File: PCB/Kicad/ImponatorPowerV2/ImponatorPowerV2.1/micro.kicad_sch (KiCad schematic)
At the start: 7 parts, among them U2 EFM8UB10F16G

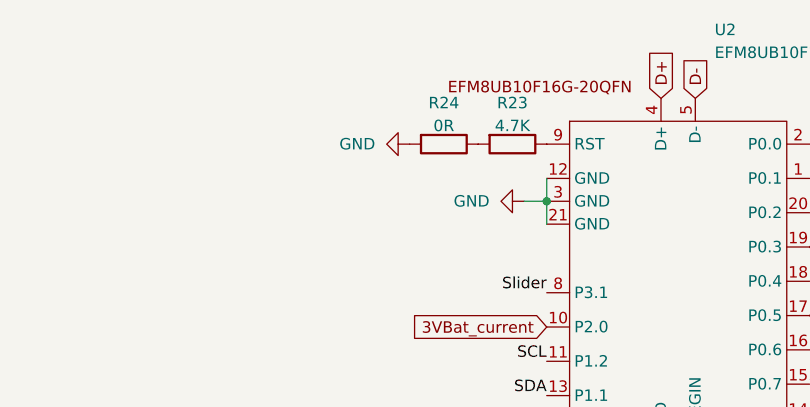
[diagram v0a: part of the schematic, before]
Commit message: 6 layer version of imponatorPower routed.
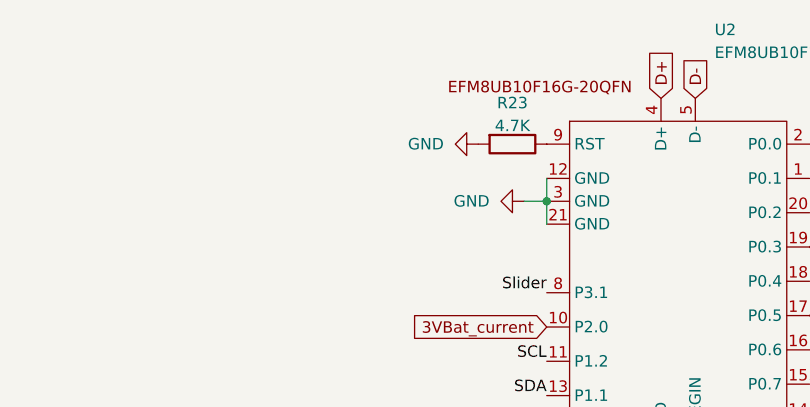
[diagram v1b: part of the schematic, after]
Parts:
- removed R24: 0R, Custom:RST, symbol Device:R
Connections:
- net GND: now also R23.2
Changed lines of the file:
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@@
 		)
 		(instances
-			(project "ImponatorPowerV2"
+			(project "ImponatorPowerV2.1"
 				(path "/39f9a456-0dc1-46da-8595-29035f4abc44/0165c1f8-8834-4f35-a624-6b8efab38fa5"
 					(reference "R23")
@@
 		)
 		(instances
-			(project "ImponatorPowerV2"
+			(project "ImponatorPowerV2.1"
 				(path "/39f9a456-0dc1-46da-8595-29035f4abc44/0165c1f8-8834-4f35-a624-6b8efab38fa5"
 					(reference "#PWR048")
-					(unit 1)
-				)
-			)
-		)
-	)
-	(symbol
-		(lib_id "Device:R")
-		(at 128.27 67.31 270)
-		(unit 1)
-		(body_style 1)
-		(exclude_from_sim no)
-		(in_bom yes)
-		(on_board yes)
-		(in_pos_files yes)
-		(dnp no)
-		(property "Reference" "R24"
-			(at 128.27 62.738 90)
-			(show_name no)
-			(do_not_autoplace no)
-			(effects
-				(font
-					(size 1.27 1.27)
-				)
-			)
-		)
-		(property "Value" "0R"
-			(at 128.27 65.278 90)
-			(show_name no)
-			(do_not_autoplace no)
-			(effects
-				(font
-					(size 1.27 1.27)
-				)
-			)
-		)
-		(property "Footprint" "Custom:RST"
-			(at 128.27 65.532 90)
-			(hide yes)
-			(show_name no)
-			(do_not_autoplace no)
-			(effects
-				(font
-					(size 1.27 1.27)
-				)
-			)
-		)
-		(property "Datasheet" ""
-			(at 128.27 67.31 0)
-			(hide yes)
-			(show_name no)
-			(do_not_autoplace no)
-			(effects
-				(font
-					(size 1.27 1.27)
-				)
-			)
-		)
-		(property "Description" "Resistor"
-			(at 128.27 67.31 0)
-			(hide yes)
-			(show_name no)
-			(do_not_autoplace no)
-			(effects
-				(font
-					(size 1.27 1.27)
-				)
-			)
-		)
-		(pin "2"
-		)
-		(pin "1"
-		)
-		(instances
-			(project "ImponatorPowerV2"
-				(path "/39f9a456-0dc1-46da-8595-29035f4abc44/0165c1f8-8834-4f35-a624-6b8efab38fa5"
-					(reference "R24")
 					(unit 1)
 				)
@@
 		)
 		(instances
-			(project "ImponatorPowerV2"
+			(project "ImponatorPowerV2.1"
 				(path "/39f9a456-0dc1-46da-8595-29035f4abc44/0165c1f8-8834-4f35-a624-6b8efab38fa5"
 					(reference "#PWR047")
@@
 		)
 		(instances
-			(project "ImponatorPowerV2"
+			(project "ImponatorPowerV2.1"
 				(path "/39f9a456-0dc1-46da-8595-29035f4abc44/0165c1f8-8834-4f35-a624-6b8efab38fa5"
 					(reference "#PWR030")
@@
 		)
 		(instances
-			(project "ImponatorPowerV2"
+			(project "ImponatorPowerV2.1"
 				(path "/39f9a456-0dc1-46da-8595-29035f4abc44/0165c1f8-8834-4f35-a624-6b8efab38fa5"
 					(reference "C10")
@@
 		)
 		(instances
-			(project "ImponatorPowerV2"
+			(project "ImponatorPowerV2.1"
 				(path "/39f9a456-0dc1-46da-8595-29035f4abc44/0165c1f8-8834-4f35-a624-6b8efab38fa5"
 					(reference "C18")
@@
 		)
 		(instances
-			(project "ImponatorPowerV2"
+			(project "ImponatorPowerV2.1"
 				(path "/39f9a456-0dc1-46da-8595-29035f4abc44/0165c1f8-8834-4f35-a624-6b8efab38fa5"
 					(reference "#PWR026")
@@
 		)
 		(instances
-			(project "ImponatorPowerV2"
+			(project "ImponatorPowerV2.1"
 				(path "/39f9a456-0dc1-46da-8595-29035f4abc44/0165c1f8-8834-4f35-a624-6b8efab38fa5"
 					(reference "U2")
@@
 		)
 		(instances
-			(project "ImponatorPowerV2"
+			(project "ImponatorPowerV2.1"
 				(path "/39f9a456-0dc1-46da-8595-29035f4abc44/0165c1f8-8834-4f35-a624-6b8efab38fa5"
 					(reference "#PWR025")
@@
 		)
 		(instances
-			(project "ImponatorPowerV2"
+			(project "ImponatorPowerV2.1"
 				(path "/39f9a456-0dc1-46da-8595-29035f4abc44/0165c1f8-8834-4f35-a624-6b8efab38fa5"
 					(reference "C19")
@@
 	(symbol
 		(lib_id "power:GND")
-		(at 124.46 67.31 270)
+		(at 132.08 67.31 270)
 		(unit 1)
 		(body_style 1)
@@
 		(fields_autoplaced yes)
 		(property "Reference" "#PWR052"
-			(at 118.11 67.31 0)
+			(at 125.73 67.31 0)
 			(hide yes)
 			(show_name no)
@@
 		)
 		(property "Value" "GND"
-			(at 120.65 67.3099 90)
+			(at 128.27 67.3099 90)
 			(show_name no)
 			(do_not_autoplace no)
@@
 		)
 		(property "Footprint" ""
-			(at 124.46 67.31 0)
+			(at 132.08 67.31 0)
 			(hide yes)
 			(show_name no)
@@
 		)
 		(property "Datasheet" ""
-			(at 124.46 67.31 0)
+			(at 132.08 67.31 0)
 			(hide yes)
 			(show_name no)
@@
 		)
 		(property "Description" "Power symbol creates a global label with name \"GND\" , ground"
-			(at 124.46 67.31 0)
+			(at 132.08 67.31 0)
 			(hide yes)
 			(show_name no)
@@
 		)
 		(instances
-			(project "ImponatorPowerV2"
+			(project "ImponatorPowerV2.1"
 				(path "/39f9a456-0dc1-46da-8595-29035f4abc44/0165c1f8-8834-4f35-a624-6b8efab38fa5"
 					(reference "#PWR052")
@@
 		)
 		(instances
-			(project "ImponatorPowerV2"
+			(project "ImponatorPowerV2.1"
 				(path "/39f9a456-0dc1-46da-8595-29035f4abc44/0165c1f8-8834-4f35-a624-6b8efab38fa5"
 					(reference "#PWR046")
@@
 		)
 		(instances
-			(project "ImponatorPowerV2"
+			(project "ImponatorPowerV2.1"
 				(path "/39f9a456-0dc1-46da-8595-29035f4abc44/0165c1f8-8834-4f35-a624-6b8efab38fa5"
 					(reference "C11")
@@
 		)
 		(instances
-			(project "ImponatorPowerV2"
+			(project "ImponatorPowerV2.1"
 				(path "/39f9a456-0dc1-46da-8595-29035f4abc44/0165c1f8-8834-4f35-a624-6b8efab38fa5"
 					(page "10")
@@
 		)
 		(instances
-			(project "ImponatorPowerV2"
+			(project "ImponatorPowerV2.1"
 				(path "/39f9a456-0dc1-46da-8595-29035f4abc44/0165c1f8-8834-4f35-a624-6b8efab38fa5"
 					(page "11")
@@
 		)
 		(instances
-			(project "ImponatorPowerV2"
+			(project "ImponatorPowerV2.1"
 				(path "/39f9a456-0dc1-46da-8595-29035f4abc44/0165c1f8-8834-4f35-a624-6b8efab38fa5"
 					(page "12")
@@
 		)
 		(instances
-			(project "ImponatorPowerV2"
+			(project "ImponatorPowerV2.1"
 				(path "/39f9a456-0dc1-46da-8595-29035f4abc44/0165c1f8-8834-4f35-a624-6b8efab38fa5"
 					(page "13")
